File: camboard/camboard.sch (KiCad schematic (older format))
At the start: 45 parts, among them J1 USB_microB_2040002-1, J2 Micro_SD_Card, J3 PPTC102LFBN-RC, J4 Conn_ARM_JTAG_SWD_20, SW1 SW_DPDT_x2, U1 STM32F746VGT6, U2 MCP1703A-3302_SOT23, U3 FT230XS, Y1 SG-310SCN, Y2 NX3215SA

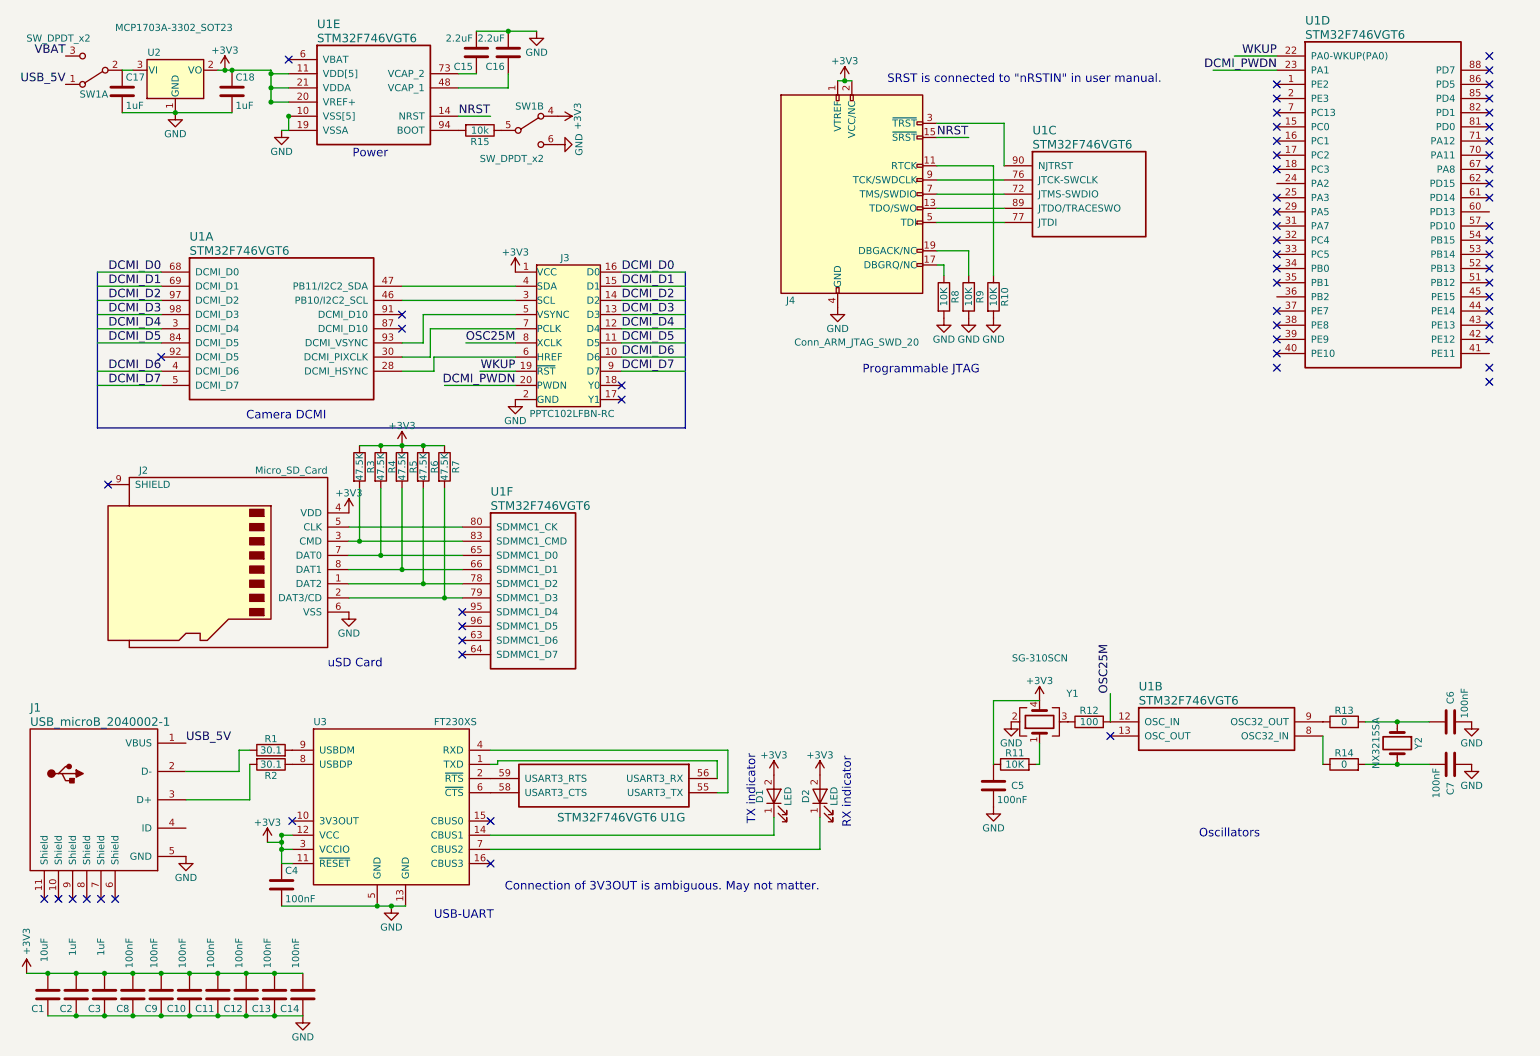
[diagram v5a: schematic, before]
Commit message: Added headers
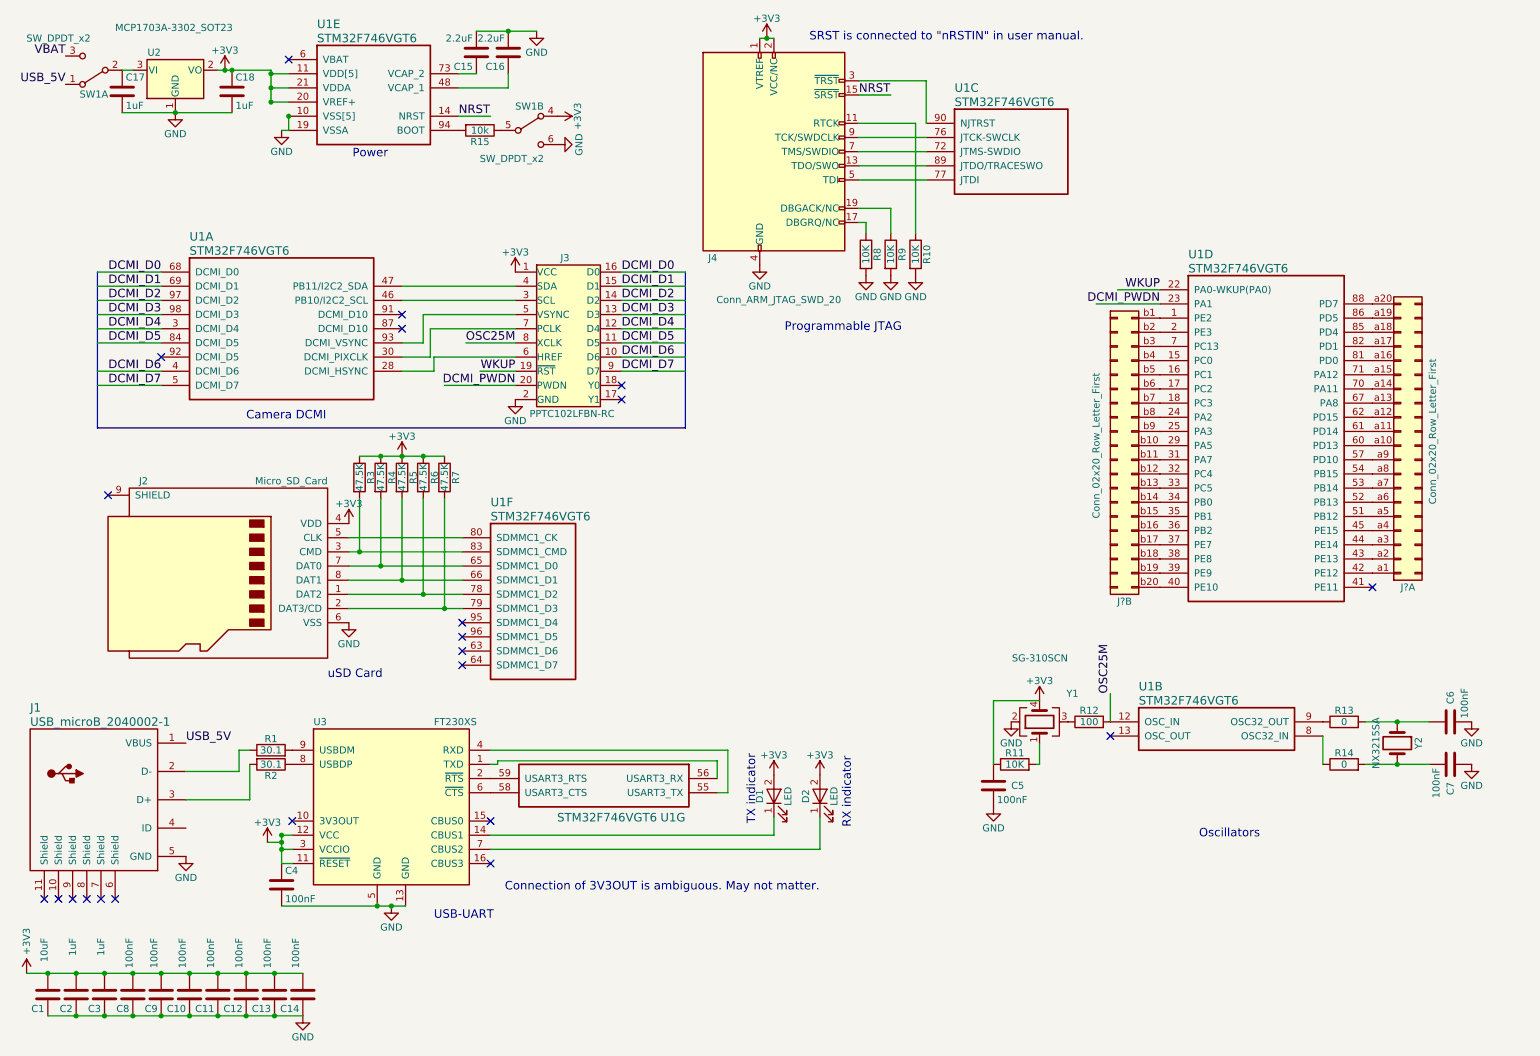
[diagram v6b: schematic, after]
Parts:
- added J? (x2): Conn_02x20_Row_Letter_First, symbol Conn_02x20_Row_Letter_First
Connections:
- no-connect marks 62 -> 22
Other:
- moved on the sheet: J2, J4, R10, R3, R4, R5, R6, R7, R8, R9, U1C, U1D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

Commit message: Added longer headers
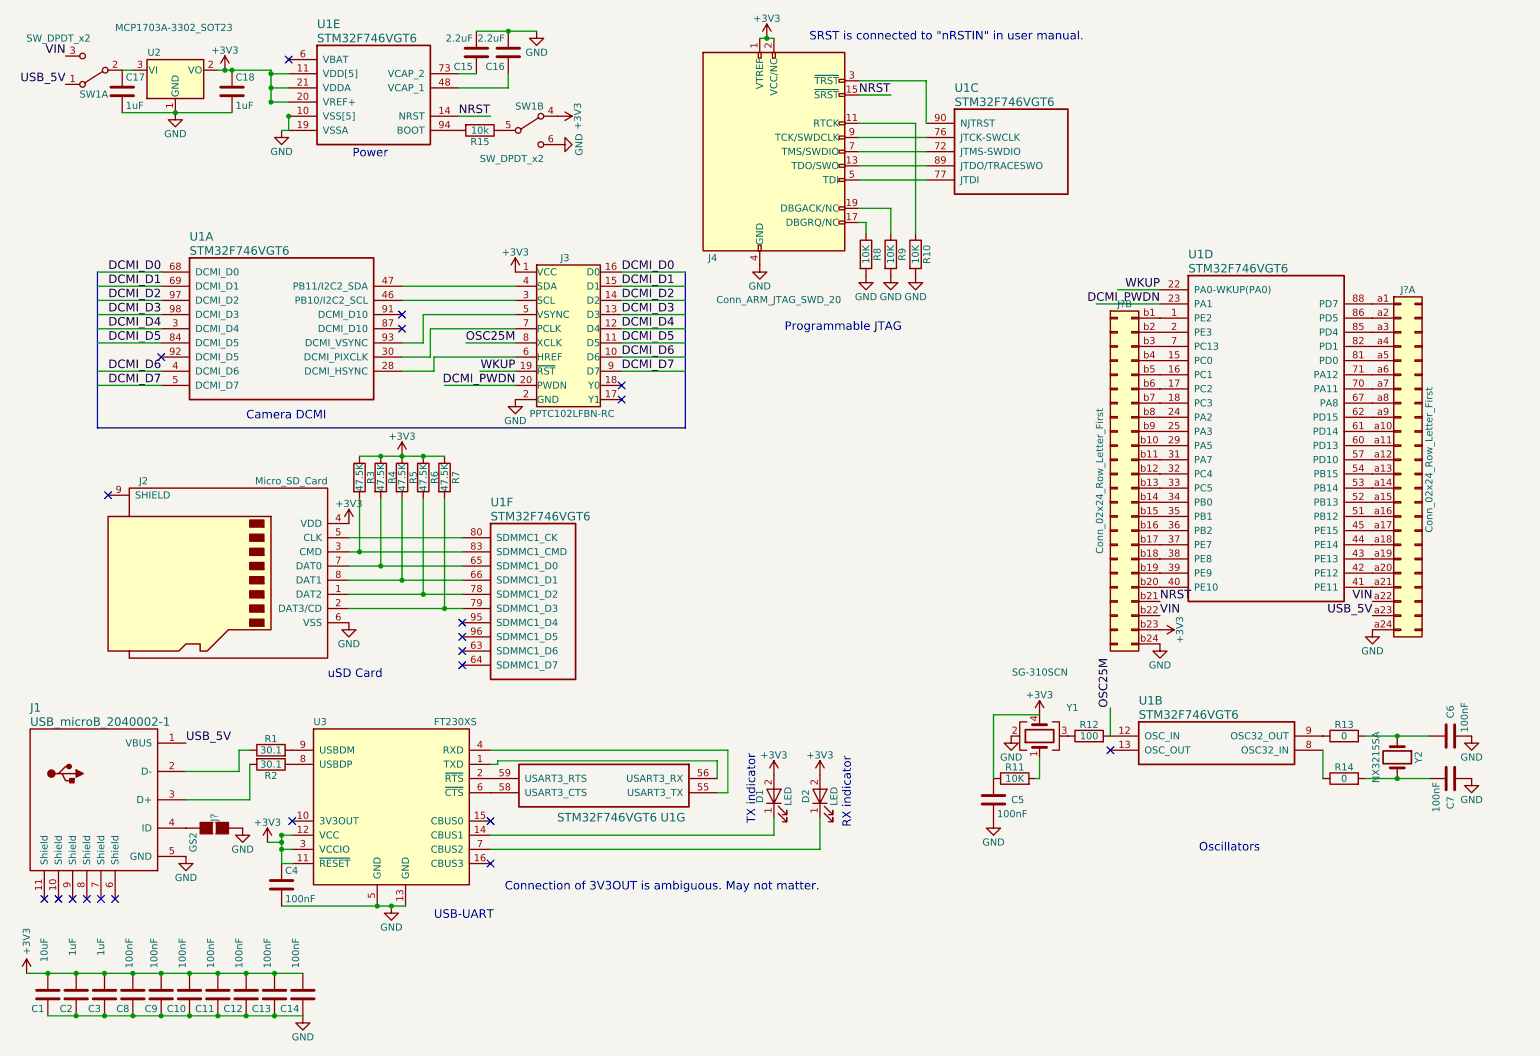
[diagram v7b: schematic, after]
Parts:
- removed J? (x2): Conn_02x20_Row_Letter_First, symbol Conn_02x20_Row_Letter_First
- added J? (x2): Conn_02x24_Row_Letter_First, symbol Conn_02x24_Row_Letter_First
- added J?: GS2, Connectors:GS2, symbol GS2
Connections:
- net labels added: VIN
- net labels removed: VBAT
- no-connect marks 22 -> 21
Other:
- moved on the sheet: C5, C6, C7, R11, R12, R13, R14, U1B, Y1, Y2

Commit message: Added user-controlled buttons and LED's
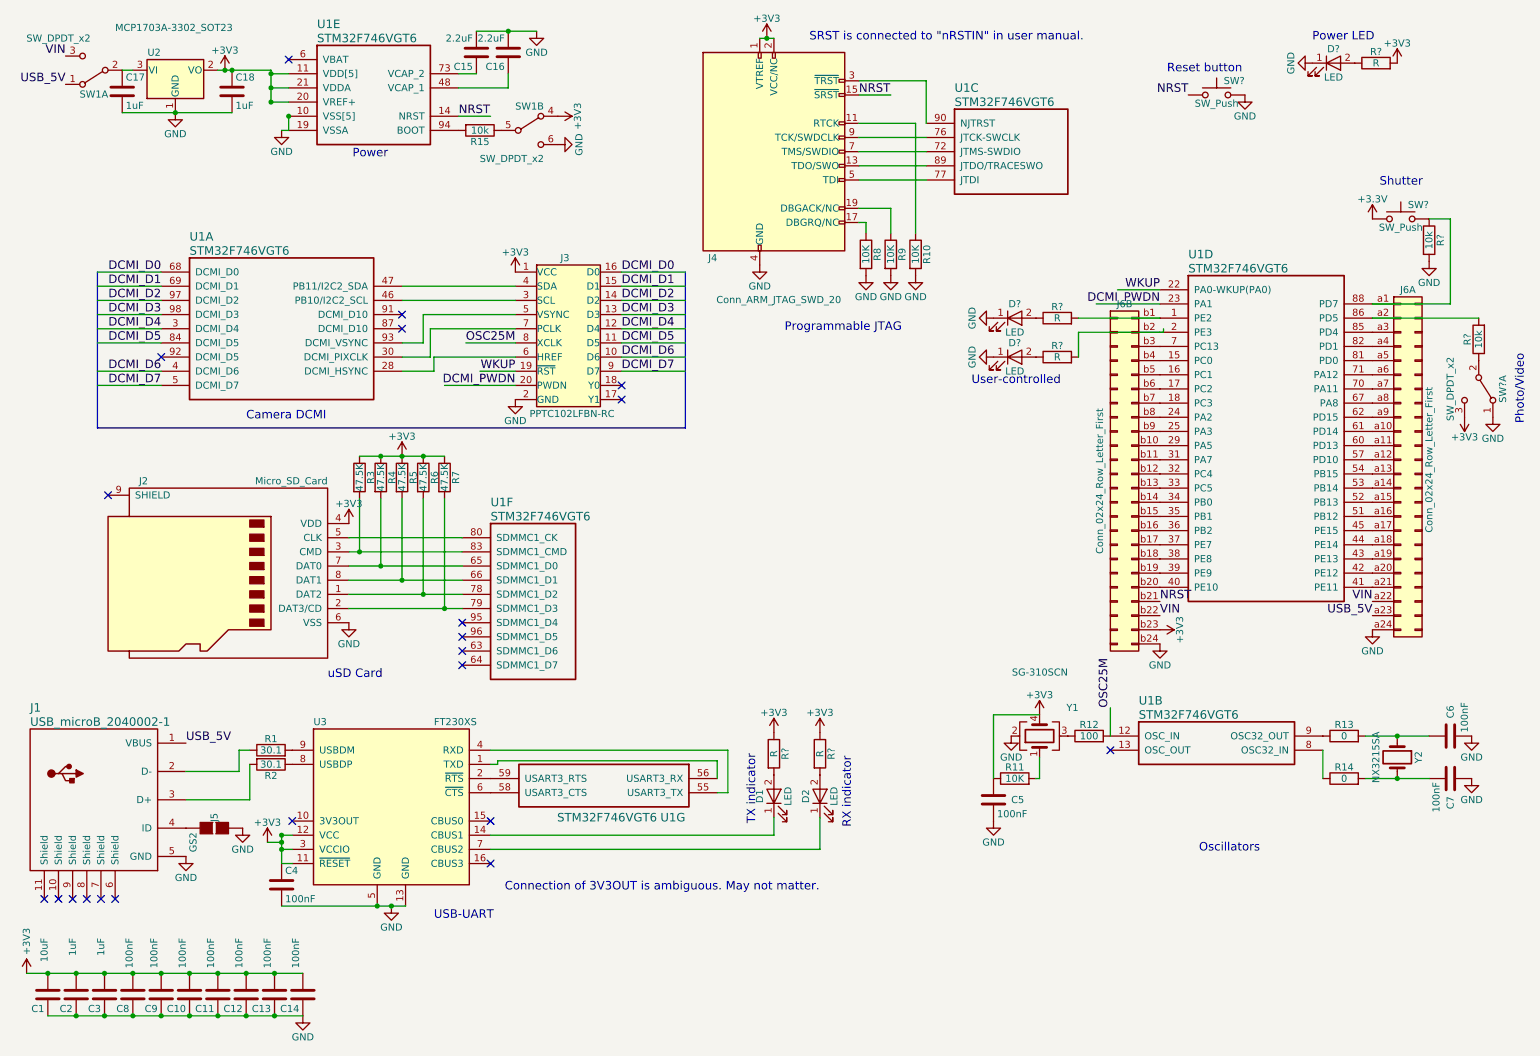
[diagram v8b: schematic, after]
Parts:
- added D? (x3): LED, symbol LED
- added R? (x2): 10k, symbol R
- added R? (x5): R, symbol R
- added SW? (x2): SW_Push, Buttons_Switches_SMD:SW_SPST_B3U-1000P, symbol SW_Push
- added SW?: SW_DPDT_x2, Buttons_Switches_THT:SW_CuK_JS202011CQN_DPDT_Straight, symbol SW_DPDT_x2
- gave numbers to parts that had none: 2
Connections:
- net labels added: +3.3V
- wire segments 104 -> 112
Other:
- note added: "Photo/Video"
- note added: "Power LED"
- note added: "Reset button"
- note added: "Shutter"
- note added: "User-controlled"
